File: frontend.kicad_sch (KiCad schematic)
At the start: 80 parts, among them P4 SMA, Q1 NMOS/PMOS, U12 BGS13SN8, U13 74LVC1G86, U14 BGS13SN8, U24 AP22652, U25 BGB741L7ESD, U37 74LVC1G86, U40 BGB741L7ESD

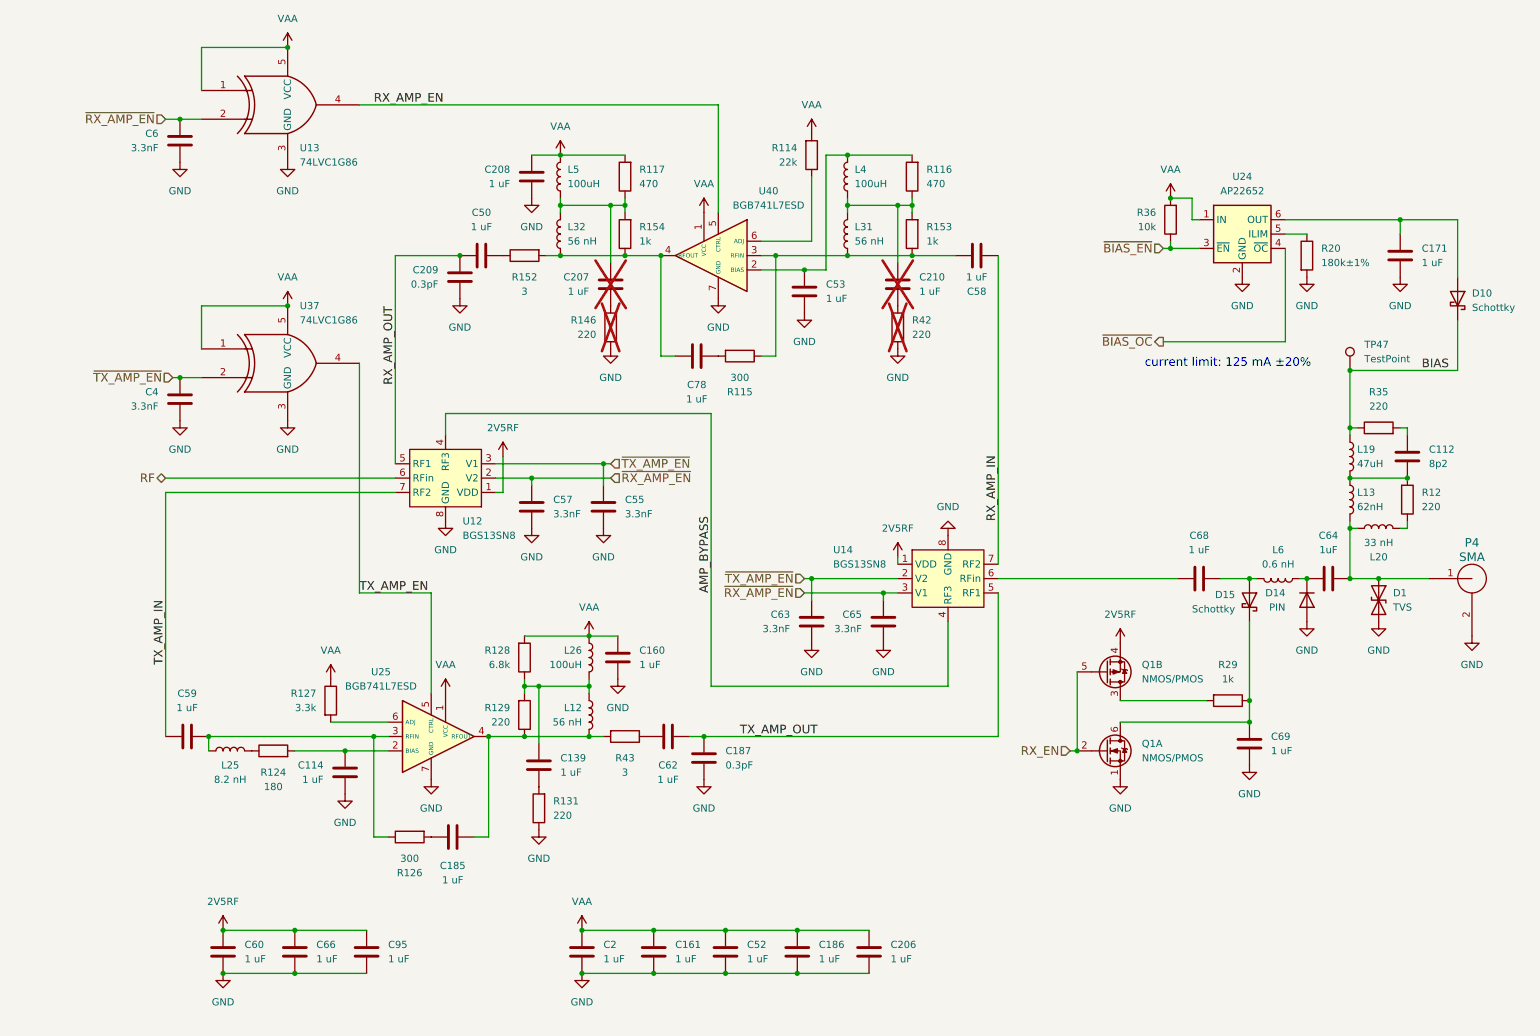
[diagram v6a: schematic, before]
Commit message: Change TX RF amplifier to TRF37C73
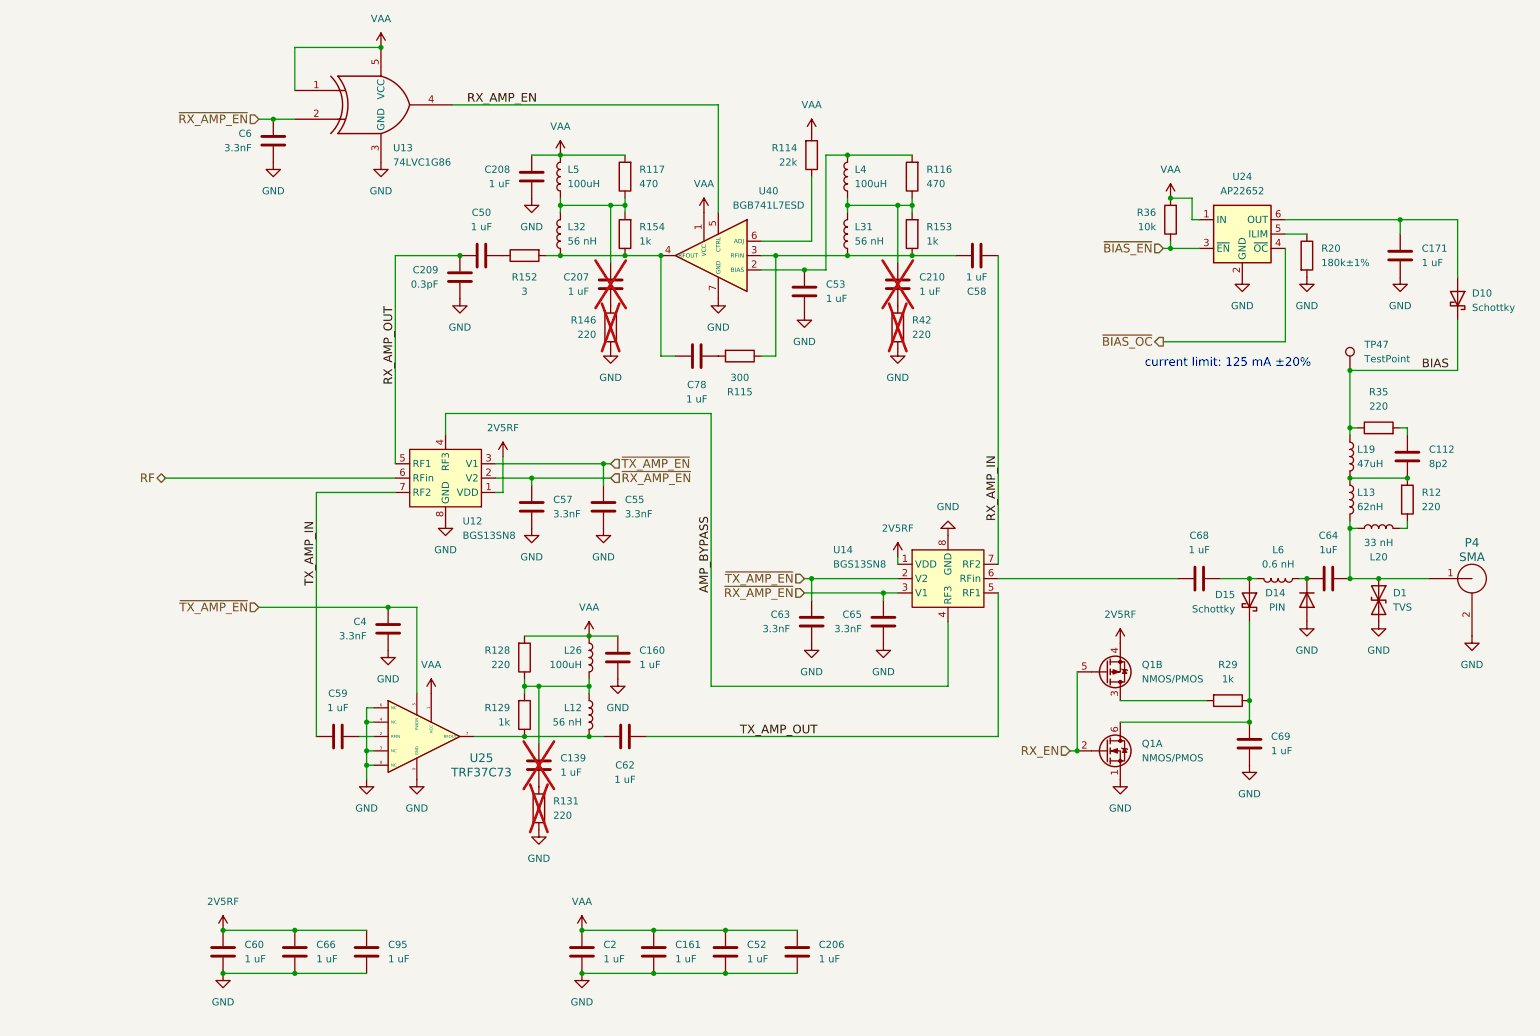
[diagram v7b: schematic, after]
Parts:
- removed C114, C185, C186: 1 uF, Capacitor_SMD:C_0201_0603Metric, symbol Device:C
- removed C187: 0.3pF, Capacitor_SMD:C_0201_0603Metric, symbol Device:C
- removed L25: 8.2 nH, Inductor_SMD:L_0201_0603Metric, symbol Device:L
- removed R124: 180, Resistor_SMD:R_0201_0603Metric, symbol Device:R
- removed R126: 300, Resistor_SMD:R_0201_0603Metric, symbol Device:R
- removed R127: 3.3k, Resistor_SMD:R_0201_0603Metric, symbol Device:R
- removed R43: 3, Resistor_SMD:R_0201_0603Metric, symbol Device:R
- removed U25: BGB741L7ESD, praline:TSLP-7-1, symbol praline:BGB741L7ESD
- removed U37: 74LVC1G86, Package_TO_SOT_SMD:SOT-353_SC-70-5, symbol 74xGxx:74LVC1G86
- added U25: TRF37C73, Package_SON:WSON-8-1EP_2x2mm_P0.5mm_EP0.9x1.6mm, symbol praline:TRF37A73
- C139, R131: now not fitted
- R128: value 6.8k -> 220; Part Number RC0201FR-076K8L -> RC0201JR-07220RL
- R129: value 220 -> 1k; Part Number RC0201JR-07220RL -> RC0201FR-071KL
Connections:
- net GND: now also U25.3 (NC), U25.4 (NC), U25.6 (NC), U25.8 (NC), U25.9 (GND)
- net VAA: now also U25.1 (VCC)
- net ~{TX_AMP_EN}: now also U25.5 (PWDN)
- net at C59.2: now also U25.2 (RFIN)
- net at C62.1: now also L12.2, R129.1, U25.7 (RFOUT)
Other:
- moved on the sheet: C206, C4, C59, C6, C62, U13

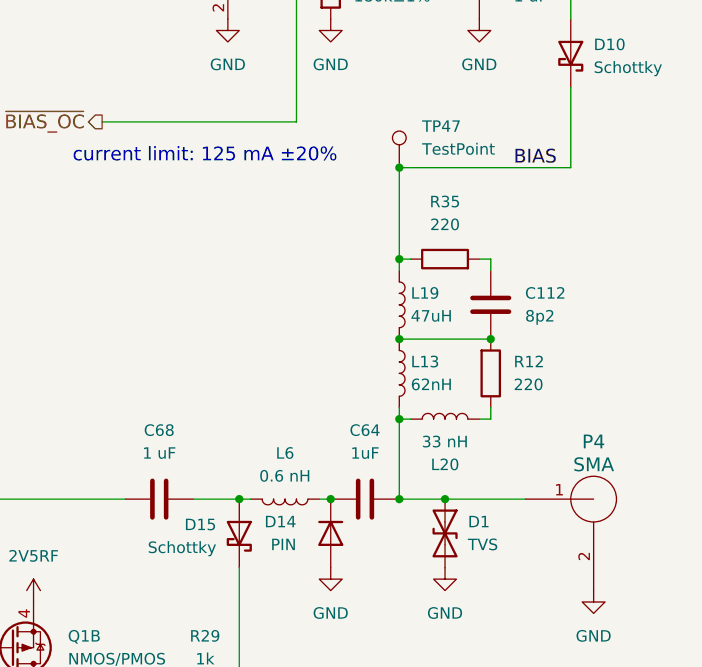
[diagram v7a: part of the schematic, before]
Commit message: Tune bias tee and limiter
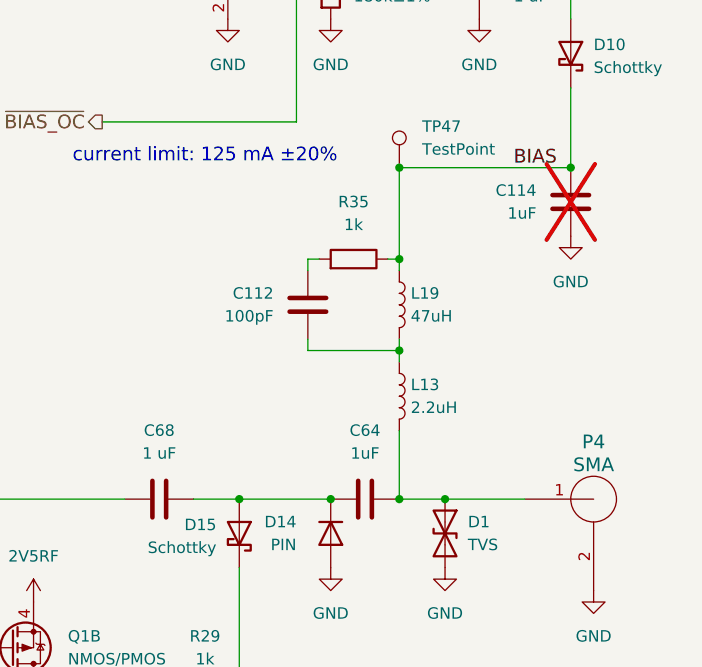
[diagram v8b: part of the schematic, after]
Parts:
- removed L20: 33 nH, Inductor_SMD:L_0201_0603Metric, symbol Device:L
- removed L6: 0.6 nH, Inductor_SMD:L_0201_0603Metric, symbol Device:L
- removed R12: 220, Resistor_SMD:R_0201_0603Metric, symbol Device:R
- added C114: 1uF, Capacitor_SMD:C_0402_1005Metric, symbol Device:C
- C112: value 8p2 -> 100pF; Part Number GRM0335C1H8R2CA01D -> GRM0335C1E101JA01D; Substitution GRM0335C1H8R2* -> GRM0335C1E101JA01*, GRM0335C1H101JA01*
- C171: footprint Capacitor_SMD:C_0201_0603Metric -> Capacitor_SMD:C_0402_1005Metric; Manufacturer Murata -> Samsung; Part Number GRM033R61A105ME44D -> CL05A105KA5NQNC; Substitution GRM033R61A105ME44*, GRM033R61C105ME15*, Samsung CL03A105MO3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 -> Murata GRM155R61E105KA12D
- L13: value 62nH -> 2.2uH; Manufacturer Murata -> Taiyo Yuden; Part Number LQW18AN62NJ00D -> LSQPB160807T2R2M; Substitution LQW18AN62N* -> BRL1608T2R2M, LLQPB160807T2R2M
- R35: value 220 -> 1k; Part Number RC0201JR-07220RL -> RC0201FR-071KL
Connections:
- net BIAS: now also C114.2
- net GND: now also C114.1
- net at C64.1, D14.1 (K): now also C68.2, D15.2 (A)
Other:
- moved on the sheet: C112, L13, R35
